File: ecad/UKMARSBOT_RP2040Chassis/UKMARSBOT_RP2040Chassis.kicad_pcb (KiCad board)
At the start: 2 copper layers, 99.1 x 81.3 mm, 24 parts, among them J1 CONN_06SILK_FEMALE_PTH, J2 CONN_06SILK_FEMALE_PTH, J3 Conn_01x06, J4 Conn_01x06, J6 POWER, J7 Switch, M1 Left MOTOR, M2 Right MOTOR, U1 DVR8833_DC_Controller, U2 LM7805_TO220

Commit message: Cap rename to maintain consistancy across all boards
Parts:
- C3: value 100uF,16V -> 100uF, 16V
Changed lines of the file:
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@@
 			)
 		)
-		(property "Value" "100uF,16V"
+		(property "Value" "100uF, 16V"
 			(at 1.25 4.4 180)
 			(layer "F.Fab")

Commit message: Last check to try and fix motor BOM issue
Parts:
- M1: value Left MOTOR -> N20 MOTOR
- M2: value Right MOTOR -> N20 MOTOR

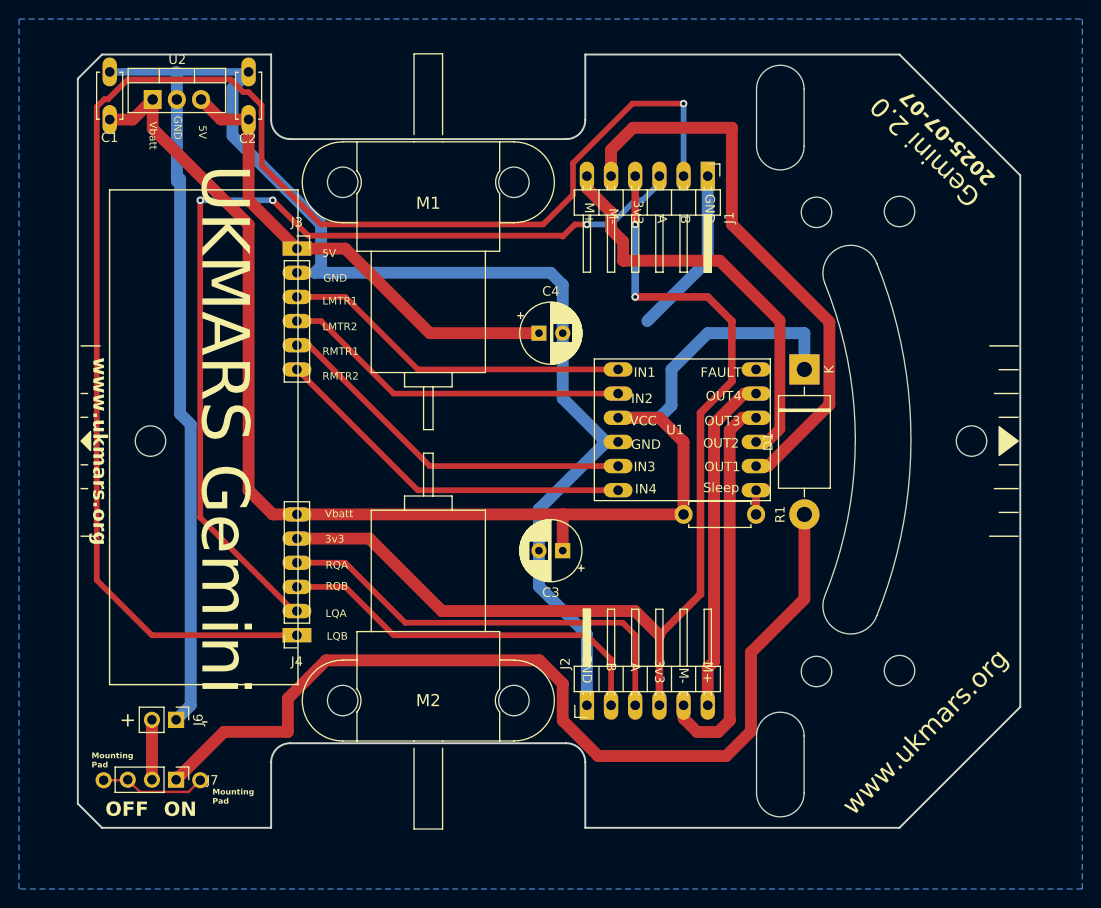
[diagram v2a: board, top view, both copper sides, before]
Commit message: Adjustments to chassis and Mez
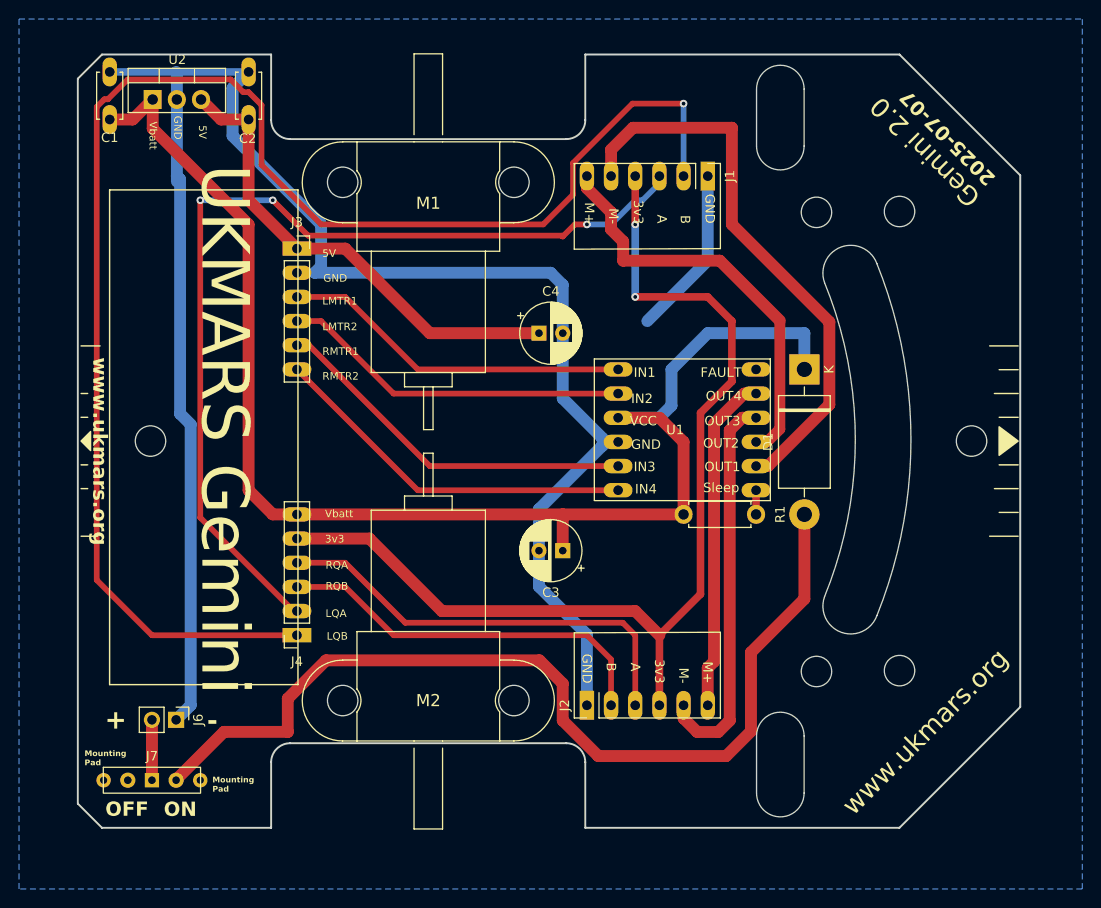
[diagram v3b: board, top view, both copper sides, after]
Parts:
- removed ? (x2): , 
- J1, J2: value CONN_06SILK_FEMALE_PTH -> Pololu Item #4772; footprint Connector_PinHeader_2.54mm:PinHeader_1x06_P2.54mm_Horizontal -> ukmarsbot:Connector_Pololu_JST-SH_side_entry_breakout
- J7: footprint Connector_PinHeader_2.54mm:PinHeader_1x03_P2.54mm_Vertical -> ukmarsbot:UKMARSBOT_SW_Slide-03_With_Mounting_Pads
- moved J7 2.54 mm to (91.4, 137.2), turned to 0 degrees
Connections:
- J7 pad 1: /PWR -> /PWR_IN
- J7 pad 2: /PWR_IN -> unconnected-(J7-Pin_2-Pad2)
- J7 pad 3: unconnected-(J7-Pin_3-Pad3) -> /PWR
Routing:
- net unconnected-(J7-Pin_3-Pad3): track 11.2 -> 0.00 mm
